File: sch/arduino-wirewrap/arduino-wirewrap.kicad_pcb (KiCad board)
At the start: 2 copper layers, 139 x 66 mm, 2 parts, among them J1 Conn_02x34_Top_Bottom

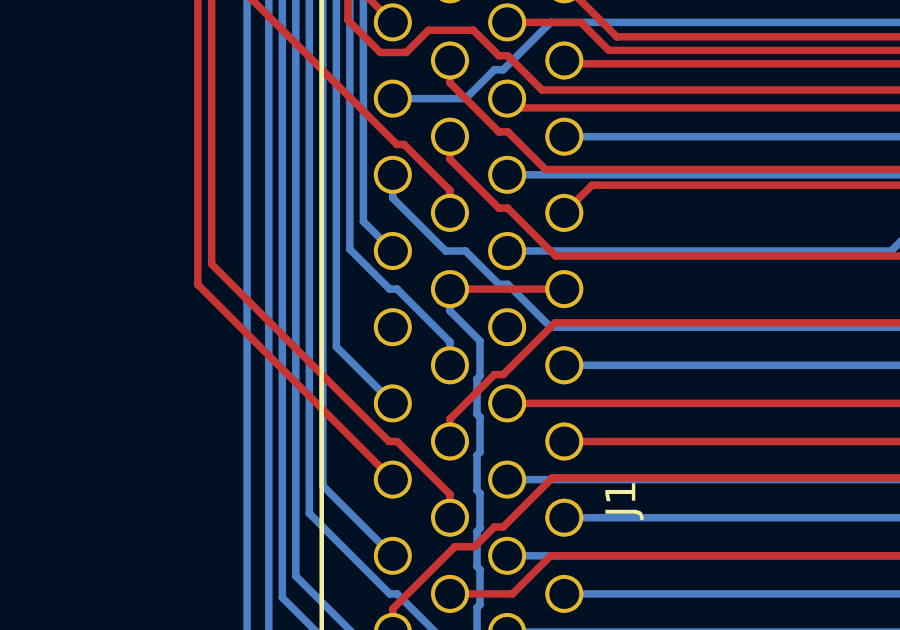
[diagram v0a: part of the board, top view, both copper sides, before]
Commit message: Connect VPP to 5V as standard says
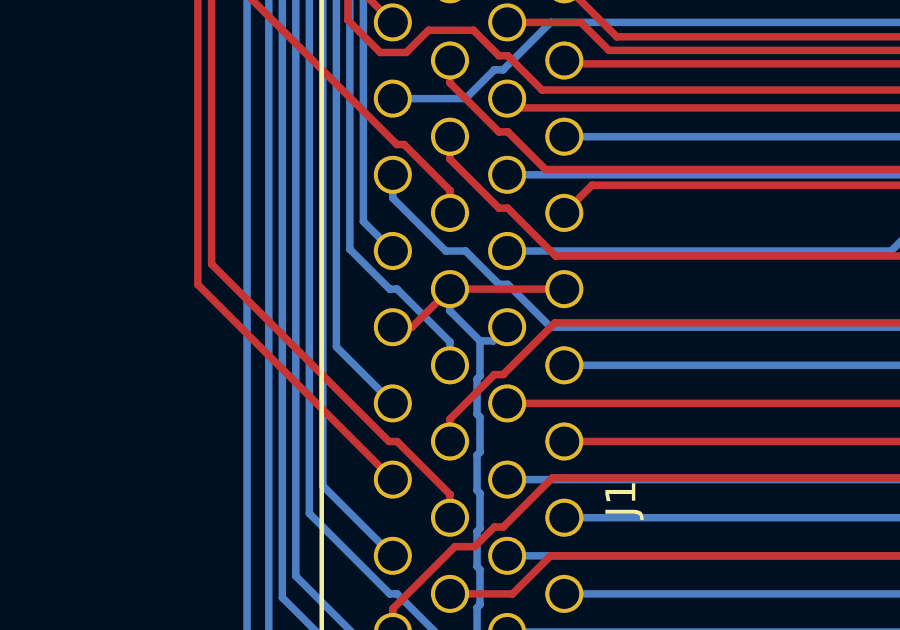
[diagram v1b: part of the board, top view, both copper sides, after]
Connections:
- J1 pad 18: Net-(J1-Pad18) -> +5V
- J1 pad 52: Net-(J1-Pad52) -> +5V
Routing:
- net +5V: track 170.7 -> 174.5 mm

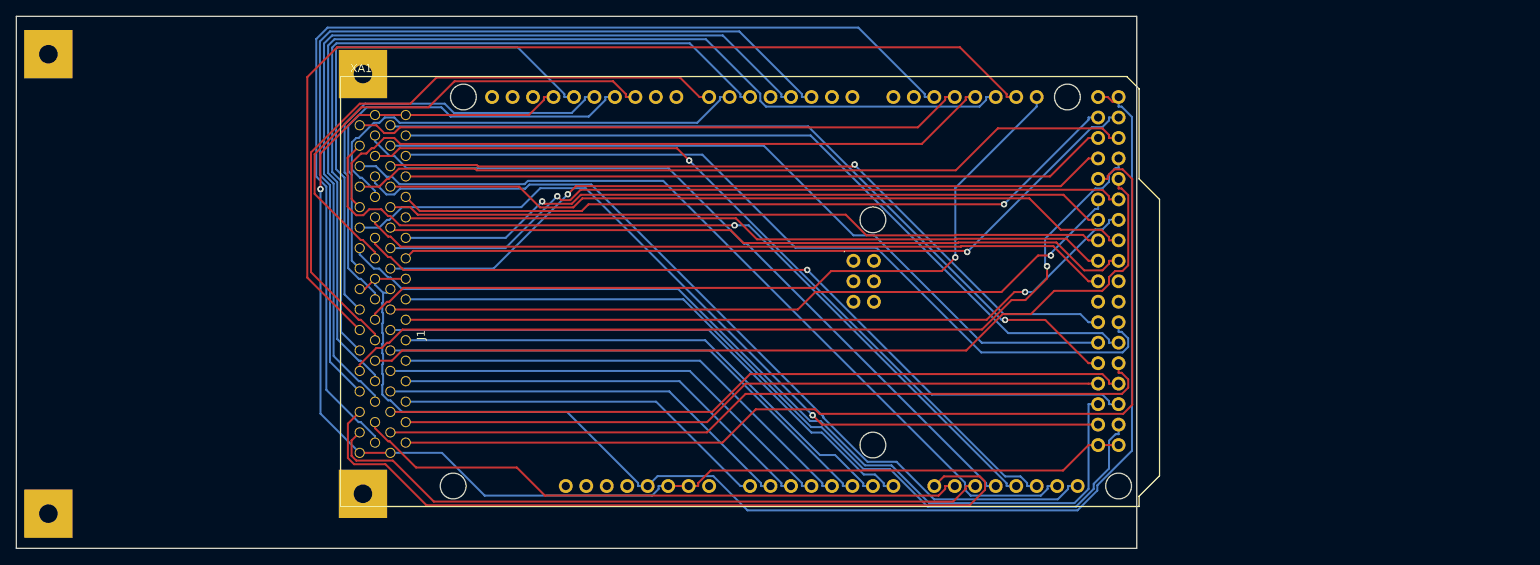
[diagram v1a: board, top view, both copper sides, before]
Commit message: Relayout board as pcmcia connectior will clash with usb connector
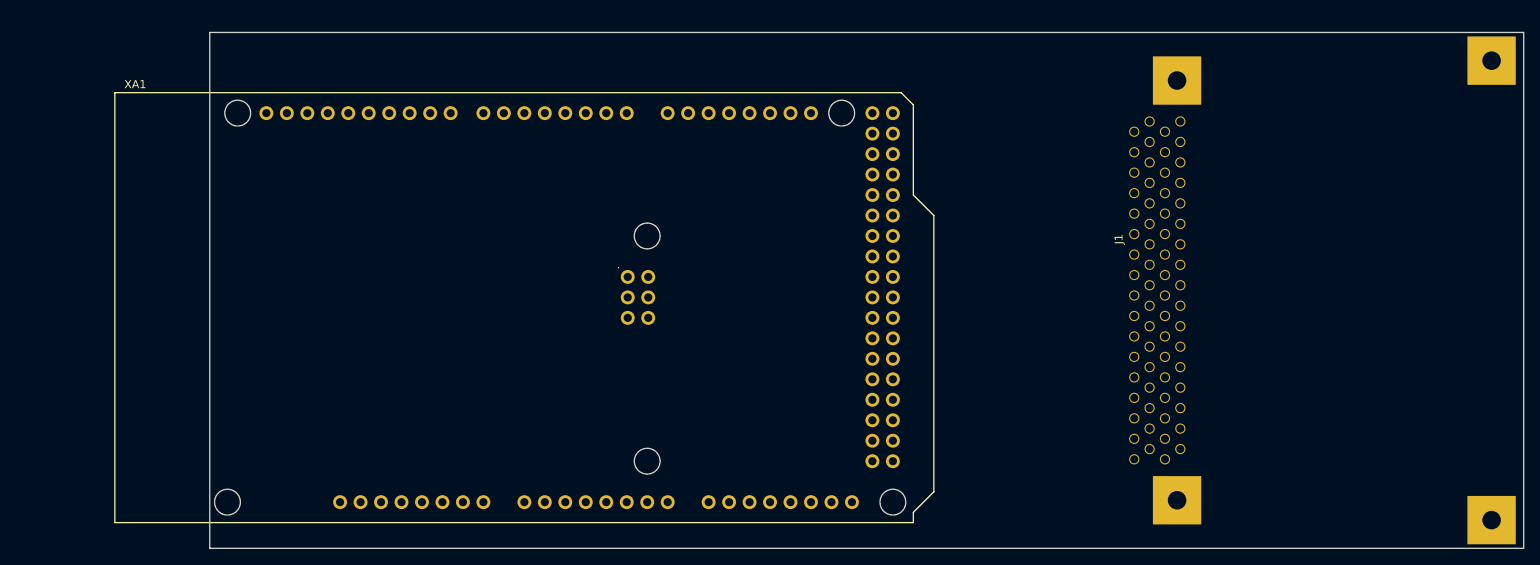
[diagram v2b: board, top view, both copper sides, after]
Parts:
- moved J1 101.0 mm to (175.0, 91.0), turned to 90 degrees
- moved XA1 28.1 mm to (43.2, 119.8)
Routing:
- net +5V: track 174.5 -> 0.00 mm
- net GND: track 170.6 -> 0.00 mm, vias 1 -> 0
- net /PH1_CD2: track 134.3 -> 0.00 mm
- net /PD2_REG: track 132.0 -> 0.00 mm
- net /PD1_A25: track 126.3 -> 0.00 mm
- net /PA6_IOIS16_WP: track 126.0 -> 0.00 mm
- net /PB3_A19: track 116.4 -> 0.00 mm
- net /PE4_BVD1: track 110.5 -> 0.00 mm
- net /PA7_WAIT: track 110.3 -> 0.00 mm
- net /PA5_INPACK: track 110.0 -> 0.00 mm, vias 1 -> 0
- net /PE5_BVD2: track 108.9 -> 0.00 mm
- net /PB0_A16: track 106.4 -> 0.00 mm
- net /PK4_D12: track 106.3 -> 0.00 mm, vias 1 -> 0
- net /PK7_D15: track 106.2 -> 0.00 mm
- net /PB1_A17: track 105.8 -> 0.00 mm, vias 1 -> 0
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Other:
- board size 139 x 66 mm -> 163 x 64 mm

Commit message: Add gerber files for V1.0 board
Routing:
- net GND: track 0.00 -> 195.4 mm
- net +5V: track 0.00 -> 130.5 mm, vias 0 -> 2
- net /PB7_A23: track 0.00 -> 127.7 mm
- net /PB4_A20: track 0.00 -> 126.8 mm, vias 0 -> 1
- net /PB5_A21: track 0.00 -> 108.3 mm, vias 0 -> 2
- net /PB6_A22: track 0.00 -> 107.9 mm
- net /PH0_CD1: track 0.00 -> 104.0 mm
- net /PH3_VS1: track 0.00 -> 100.1 mm, vias 0 -> 1
- net /PK2_D10: track 0.00 -> 99.6 mm, vias 0 -> 1
- net /PF0_A0: track 0.00 -> 95.0 mm
- net /PF1_A1: track 0.00 -> 92.1 mm, vias 0 -> 1
- net /PH4_VS2: track 0.00 -> 91.0 mm
- net /PD3_IORD: track 0.00 -> 89.3 mm, vias 0 -> 1
- net /PE3_RESET: track 0.00 -> 88.4 mm, vias 0 -> 1
- net /PF2_A2: track 0.00 -> 86.8 mm
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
